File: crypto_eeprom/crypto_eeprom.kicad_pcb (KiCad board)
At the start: 2 copper layers, 12.8 x 9.5 mm, 3 parts, among them J1 EXPANSION_BOTTOM, U1 ATSHA204A

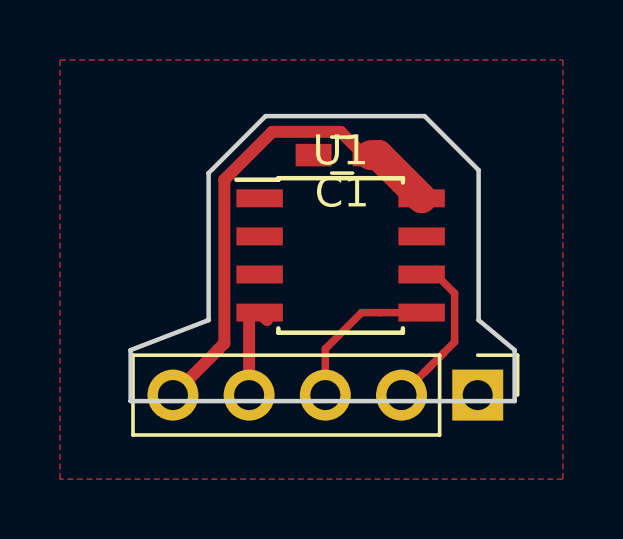
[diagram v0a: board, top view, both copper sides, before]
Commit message: Redesigned to use new footprint and UDFN IC
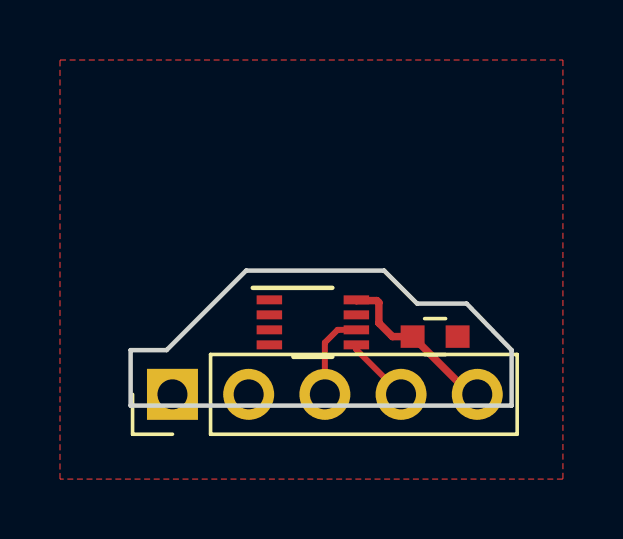
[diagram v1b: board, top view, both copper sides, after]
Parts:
- C1: footprint Capacitors_SMD:C_0603_HandSoldering -> Capacitors_SMD:C_0603
- U1: footprint Housings_SOIC:SOIC-8_3.9x4.9mm_Pitch1.27mm -> footprints:DFN-8_3x2mm_Pitch0.5mm
- moved J1 10.2 mm to (143.2, 111.5), turned to 90 degrees
- moved C1 6.80 mm to (151.9, 109.5), turned to 0 degrees
- moved U1 2.41 mm to (147.9, 109.1)
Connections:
- J1 pad 1: (no net) -> GND
- J1 pad 2: SCL -> (no net)
- J1 pad 3: SDA -> SCL
- J1 pad 4: GND -> SDA
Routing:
- net VCC: track 16.0 -> 5.75 mm
- net SDA: track 5.25 -> 2.27 mm
- net GND: track 2.85 -> 0.00 mm
- net SCL: track 6.41 -> 3.66 mm
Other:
- board size 12.8 x 9.5 mm -> 12.7 x 4.5 mm
- board text removed: "ATSHA204 ZeroPhone mod"
